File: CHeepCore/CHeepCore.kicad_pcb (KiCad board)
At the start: 2 copper layers, 29.5 x 18.3 mm, 17 parts, among them J101 Conn_01x10, J102 Conn_01x10, J201 Conn_01x03, J301 USB_C_Receptacle_USB2.0_16P, U101 CH32V003FxUx, U301 3V3 LDO, Y101 Crystal_GND24

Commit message: Added USB to smd pad
USB smd pads added on the back
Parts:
- added J103: USB, Connector_PinHeader_1.00mm:PinHeader_2x01_P1.00mm_Vertical_SMD, B.Cu at (27.2, 31.2)
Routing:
- net GND: track 12.7 -> 16.0 mm
- net /USB with LDO/D-: track 5.36 -> 8.04 mm
- net /USB with LDO/D+: track 3.89 -> 5.76 mm
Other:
- board text added: "D+"
- board text added: "D-"
- board text added: "v0.0.1c"
- board text removed: "v0.0.1b"

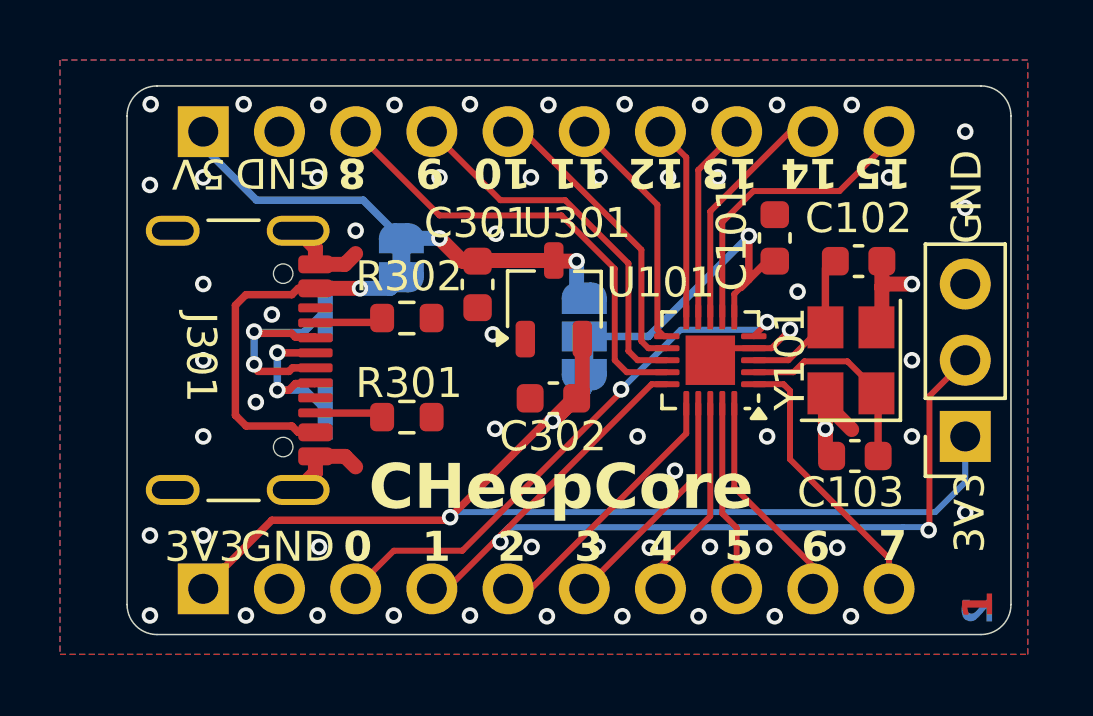
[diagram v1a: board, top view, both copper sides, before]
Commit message: Changed to TSSOP Footprint
Changed to WCH CH32V003F4P6
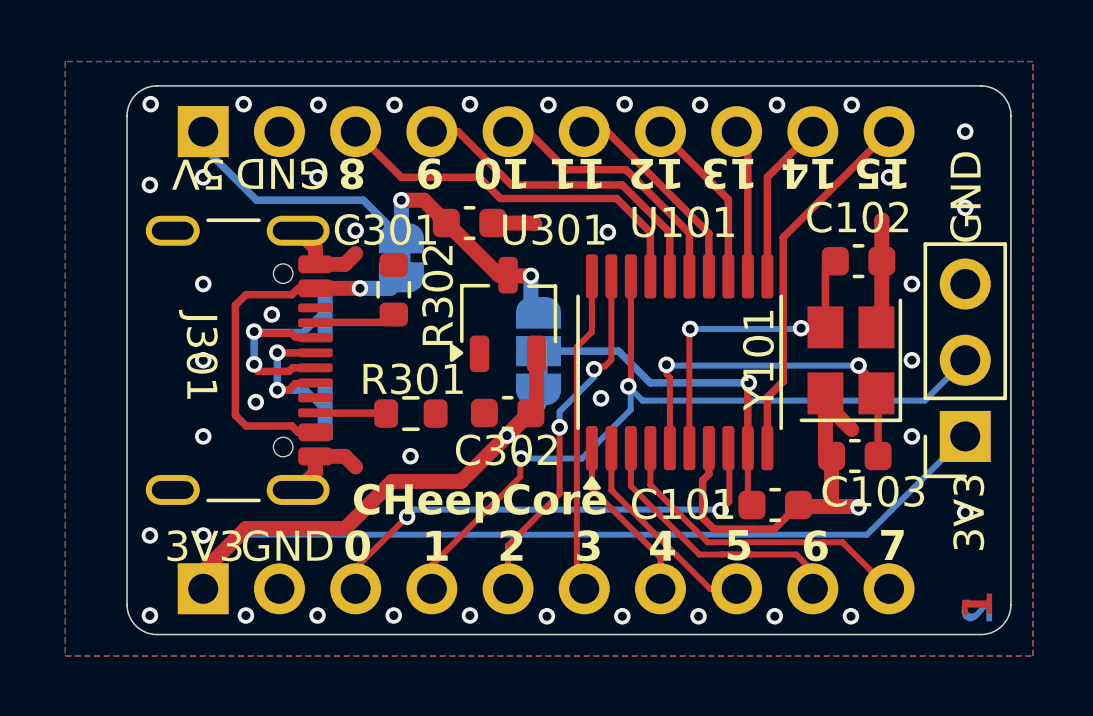
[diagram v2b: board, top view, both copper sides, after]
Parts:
- U101: value CH32V003FxUx -> CH32V003FxPx; footprint Package_DFN_QFN:QFN-20-1EP_3x3mm_P0.4mm_EP1.65x1.65mm -> Package_SO:TSSOP-20_4.4x6.5mm_P0.65mm
- moved C101 8.90 mm to (42.2, 36.1), turned to 0 degrees
- moved C301 2.06 mm to (32.0, 26.7), turned to 0 degrees
- moved JP101 1.60 mm to (34.3, 30.9)
- moved U301 1.60 mm to (33.3, 29.7)
- moved C302 1.60 mm to (33.3, 33.0)
- moved R302 1.04 mm to (29.5, 28.9), turned to 90 degrees
- moved U101 1.02 mm to (39.0, 31.3), turned to 90 degrees
- moved R301 0.18 mm to (30.0, 33.0)
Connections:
- U101 pad 1: /PD7 -> /PD4
- U101 pad 10: /PC3 -> /PC0
- U101 pad 11: /PC4 -> /PC1
- U101 pad 12: /PC5 -> /PC2
- U101 pad 13: /PC6 -> /PC3
- U101 pad 14: /PC7 -> /PC4
- U101 pad 15: /PD1 -> /PC5
- U101 pad 16: /PD2 -> /PC6
- U101 pad 17: /PD3 -> /PC7
- U101 pad 18: /PD4 -> /PD1
- U101 pad 19: /PD5 -> /PD2
- U101 pad 2: Net-(U101-PA1) -> /PD5
- U101 pad 20: /PD6 -> /PD3
- U101 pad 3: Net-(U101-PA2) -> /PD6
- U101 pad 4: GND -> /PD7
- U101 pad 5: /PD0 -> Net-(U101-PA1)
- U101 pad 6: Net-(JP101-C) -> Net-(U101-PA2)
- U101 pad 7: /PC0 -> GND
- U101 pad 8: /PC1 -> /PD0
- U101 pad 9: /PC2 -> Net-(JP101-C)
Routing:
- net GND: track 16.0 -> 24.5 mm, vias 59 -> 42
- net +3V3: track 40.4 -> 46.9 mm, vias 2 -> 1
- net Net-(U101-PA2): track 4.79 -> 10.5 mm, vias 0 -> 2
- net Net-(U101-PA1): track 6.97 -> 12.6 mm, vias 0 -> 2
- net /PD1: track 31.6 -> 26.4 mm
- net /PC1: track 8.79 -> 5.45 mm
- net /PD3: track 7.74 -> 10.7 mm
- net /PD2: track 9.08 -> 12.0 mm, vias 0 -> 2
- net /PC7: track 15.5 -> 12.7 mm
- net /PC0: track 10.2 -> 12.2 mm
- net /PC6: track 12.7 -> 10.8 mm
- net /PD6: track 7.25 -> 9.10 mm
- net /PC2: track 6.70 -> 4.98 mm
- net /PD7: track 9.27 -> 10.6 mm
- net /PD0: track 18.1 -> 16.8 mm
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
